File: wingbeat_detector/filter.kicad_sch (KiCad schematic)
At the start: 17 parts, among them J2 CONN_UMC_JACK_SMD, U2 UAF42_SMA

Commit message: Finished layout for v3.0
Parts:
- J2: value CONN_UMC_JACK_SMD -> UMC_JACK_SMD
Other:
- company: Howard Hughes Medical Institute -> Peter Polidoro
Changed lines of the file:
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@@
   (title_block
     (title "wingbeat_detector")
-    (date "2023-03-22")
+    (date "2023-03-23")
     (rev "3.0")
-    (company "Howard Hughes Medical Institute")
+    (company "Peter Polidoro")
   )
   (junction (at 106.68 50.8) (diameter 0) (color 0 0 0 0)
@@
       (effects (font (size 1.27 1.27)) (justify left))
     )
-    (property "Value" "CONN_UMC_JACK_SMD" (at 234.061 104.14 90)
-      (effects (font (size 1.27 1.27)) hide)
-    )
+    (property "Value" "UMC_JACK_SMD" (at 234.061 104.14 90)
+      (effects (font (size 1.27 1.27)) hide)
+    )

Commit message: More progress towards v4
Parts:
- removed RV1: 500k, Janelia:Potentiometer_Bourns_3223W_Vertical, symbol Janelia:R_Potentiometer_500k_3.9x3.18mm_11turn_Vertical
- added R14: GAIN1, Janelia:R_1206_3216Metric, symbol Janelia:R_150k_1206
- renumbered C9 to C6, C9 to C7, C9 to C8
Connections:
- net HIGHPASS_AMPLIFIED: now also R14.2
- net at R9.1, U2.6 (AAin-): now also R14.1
- no-connect marks 4 -> 3
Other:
- note added: "Vout/Vin = GAIN1 = Ra/Rb + 1 Low Gain: 5k/249 + 1 = 21 High Gain: 500k/249 + 1 = 2009"
- note removed: "Vout/Vin = Gain = Ra/Rb + 1 Min Gain: 5k/249 + 1 = 21 Max Gain: 500k/249 + 1 = 2009"
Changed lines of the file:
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@@
   (title_block
     (title "wingbeat_detector")
-    (date "2023-10-05")
+    (date "2023-12-08")
     (rev "4.0")
     (company "Peter Polidoro")
@@
   (junction (at 167.64 53.34) (diameter 0) (color 0 0 0 0)
   )
-  (junction (at 180.34 78.74) (diameter 0) (color 0 0 0 0)
-  )
-  (junction (at 180.34 154.94) (diameter 0) (color 0 0 0 0)
+  (junction (at 189.23 78.74) (diameter 0) (color 0 0 0 0)
+  )
+  (junction (at 189.23 154.94) (diameter 0) (color 0 0 0 0)
   )
   (no_connect (at 138.43 60.96))
-  (no_connect (at 177.8 53.34))
   (no_connect (at 101.6 85.09))
   (no_connect (at 101.6 161.29))
@@
     (stroke (width 0) (type default))
   )
-  (wire (pts (xy 180.34 46.99) (xy 180.34 78.74))
-    (stroke (width 0) (type default))
-  )
-  (wire (pts (xy 173.99 46.99) (xy 180.34 46.99))
+  (wire (pts (xy 189.23 53.34) (xy 189.23 78.74))
     (stroke (width 0) (type default))
   )
@@
     (stroke (width 0) (type default))
   )
-  (wire (pts (xy 157.48 154.94) (xy 180.34 154.94))
+  (wire (pts (xy 157.48 154.94) (xy 189.23 154.94))
     (stroke (width 0) (type default))
   )
@@
     (stroke (width 0) (type default))
   )
-  (wire (pts (xy 180.34 154.94) (xy 180.34 129.54))
+  (wire (pts (xy 189.23 154.94) (xy 189.23 129.54))
     (stroke (width 0) (type default))
   )
@@
     (stroke (width 0) (type default))
   )
-  (wire (pts (xy 157.48 78.74) (xy 180.34 78.74))
+  (wire (pts (xy 157.48 78.74) (xy 189.23 78.74))
     (stroke (width 0) (type default))
   )
@@
     (stroke (width 0) (type default))
   )
-  (wire (pts (xy 146.05 129.54) (xy 180.34 129.54))
+  (wire (pts (xy 146.05 129.54) (xy 189.23 129.54))
     (stroke (width 0) (type default))
   )
@@
     (stroke (width 0) (type default))
   )
+  (wire (pts (xy 182.88 53.34) (xy 189.23 53.34))
+    (stroke (width 0) (type default))
+  )
   (wire (pts (xy 72.39 86.36) (xy 72.39 83.82))
     (stroke (width 0) (type default))
   )
-  (wire (pts (xy 180.34 154.94) (xy 182.88 154.94))
+  (wire (pts (xy 189.23 154.94) (xy 191.77 154.94))
     (stroke (width 0) (type default))
   )
@@
     (stroke (width 0) (type default))
   )
-  (wire (pts (xy 180.34 78.74) (xy 182.88 78.74))
+  (wire (pts (xy 189.23 78.74) (xy 191.77 78.74))
     (stroke (width 0) (type default))
   )
@@
   )
   (wire (pts (xy 121.92 127) (xy 121.92 134.62))
-    (stroke (width 0) (type default))
-  )
-  (wire (pts (xy 173.99 46.99) (xy 173.99 49.53))
     (stroke (width 0) (type default))
   )
@@
     (effects (font (size 1.27 1.27)) (justify left bottom))
   )
-  (text "Vout/Vin = Gain = Ra/Rb + 1\nMin Gain: 5k/249 + 1 = 21\nMax Gain: 500k/249 + 1 = 2009 "
-    (at 166.37 44.45 0)
+  (text "Vout/Vin = GAIN1 = Ra/Rb + 1\nLow Gain: 5k/249 + 1 = 21\nHigh Gain: 500k/249 + 1 = 2009 "
+    (at 161.29 49.53 0)
     (effects (font (size 1.27 1.27)) (justify left bottom))
   )
@@
     (effects (font (size 1.27 1.27)) (justify left bottom))
   )
-  (label "BANDPASS_BUFFERED" (at 182.88 154.94 0) (fields_autoplaced)
+  (label "BANDPASS_BUFFERED" (at 191.77 154.94 0) (fields_autoplaced)
     (effects (font (size 1.27 1.27)) (justify left bottom))
   )
@@
     (effects (font (size 1.27 1.27)) (justify left bottom))
   )
-  (label "HIGHPASS_AMPLIFIED" (at 182.88 78.74 0) (fields_autoplaced)
+  (label "HIGHPASS_AMPLIFIED" (at 191.77 78.74 0) (fields_autoplaced)
     (effects (font (size 1.27 1.27)) (justify left bottom))
   )
@@
   (symbol (lib_id "Janelia:C_0.1uF_0402") (at 80.01 91.44 0) (unit 1)
     (in_bom yes) (on_board yes) (dnp no)
-    (property "Reference" "C9" (at 80.01 88.9 0)
+    (property "Reference" "C8" (at 80.01 88.9 0)
       (effects (font (size 1.016 1.016)) (justify left))
     )
@@
   (symbol (lib_id "Janelia:C_0.1uF_0402") (at 72.39 167.64 0) (unit 1)
     (in_bom yes) (on_board yes) (dnp no)
-    (property "Reference" "C9" (at 72.39 165.1 0)
+    (property "Reference" "C7" (at 72.39 165.1 0)
       (effects (font (size 1.016 1.016)) (justify left))
     )
@@
     )
   )
+  (symbol (lib_id "Janelia:R_150k_1206") (at 176.53 53.34 90) (unit 1)
+    (in_bom yes) (on_board yes) (dnp no)
+    (property "Reference" "R14" (at 176.53 50.8 90) (do_not_autoplace)
+      (effects (font (size 1.016 1.016)))
+    )
+    (property "Value" "GAIN1" (at 176.53 53.34 90) (do_not_autoplace)
+      (effects (font (size 0.762 0.762)))
+    )
+    (property "Footprint" "Janelia:R_1206_3216Metric" (at 176.53 55.118 90)
+      (effects (font (size 0.762 0.762)) hide)
+    )
+    (property "Datasheet" "" (at 176.53 51.308 90)
+      (effects (font (size 0.762 0.762)))
+    )
+    (property "Vendor" "Digi-Key" (at 173.99 48.768 90)
+      (effects (font (size 1.524 1.524)) hide)
+    )
+    (property "Vendor Part Number" "P150KBCCT-ND" (at 171.45 46.228 90)
+      (effects (font (size 1.524 1.524)) hide)
+    )
+    (property "Description" "RES SMD 150K OHM 0.1% 1/4W" (at 168.91 43.688 90)
+      (effects (font (size 1.524 1.524)) hide)
+    )
+    (property "Package" "1206" (at 176.53 53.34 0)
+      (effects (font (size 1.27 1.27)) hide)
+    )
+    (property "Manufacturer" "Panasonic Electronic Components" (at 176.53 53.34 0)
+      (effects (font (size 1.27 1.27)) hide)
+    )
+    (property "Manufacturer Part Number" "ERA-8AEB154V" (at 176.53 53.34 0)
+      (effects (font (size 1.27 1.27)) hide)
+    )
+    (pin "1")
+    (pin "2")
+    (instances
+      (project "wingbeat_detector"
+        (path "/cc457ebc-4af6-4663-b19f-8cb38f061cb4/6f9841bf-b0ef-48ff-bf2c-2bd611c72bf3"
+          (reference "R14") (unit 1)
+        )
+        (path "/cc457ebc-4af6-4663-b19f-8cb38f061cb4/6cde90e6-6156-42e3-aaac-c45ad2bfab8b"
+          (reference "R10") (unit 1)
+        )
+      )
+    )
+  )
   (symbol (lib_id "Janelia:R_49.9k_0402") (at 132.08 127 90) (unit 1)
     (in_bom yes) (on_board yes) (dnp no)
@@
     )
   )
-  (symbol (lib_id "Janelia:R_Potentiometer_500k_3.9x3.18mm_11turn_Vertical") (at 173.99 53.34 90) (unit 1)
-    (in_bom yes) (on_board yes) (dnp no)
-    (property "Reference" "RV1" (at 173.99 55.88 90)
-      (effects (font (size 1.27 1.27)))
-    )
-    (property "Value" "500k" (at 173.99 53.34 90)
-      (effects (font (size 1.27 1.27)))
-    )
-    (property "Footprint" "Janelia:Potentiometer_Bourns_3223W_Vertical" (at 156.21 53.34 0)
-      (effects (font (size 1.27 1.27)) hide)
-    )
-    (property "Datasheet" "~" (at 189.23 53.34 0)
-      (effects (font (size 1.27 1.27)) hide)
-    )
-    (property "Manufacturer" "Bourns Inc." (at 191.77 53.34 0)
-      (effects (font (size 1.27 1.27)) hide)
-    )
-    (property "Manufacturer Part Number" "3223W-1-504E" (at 158.75 53.34 0)
-      (effects (font (size 1.27 1.27)) hide)
-    )
-    (property "Description" "TRIMMER 500K OHM 0.125W J LEAD" (at 153.67 53.34 0)
-      (effects (font (size 1.27 1.27)) hide)
-    )
-    (property "Vendor" "Digi-Key" (at 186.69 53.34 0)
-      (effects (font (size 1.27 1.27)) hide)
-    )
-    (property "Vendor Part Number" "3223W-1-504ECT-ND" (at 161.29 53.34 0)
-      (effects (font (size 1.27 1.27)) hide)
-    )
-    (pin "1")
-    (pin "2")
-    (pin "3")
-    (instances
-      (project "wingbeat_detector"
-        (path "/cc457ebc-4af6-4663-b19f-8cb38f061cb4/6f9841bf-b0ef-48ff-bf2c-2bd611c72bf3"
-          (reference "RV1") (unit 1)
-        )
-        (path "/cc457ebc-4af6-4663-b19f-8cb38f061cb4/6cde90e6-6156-42e3-aaac-c45ad2bfab8b"
-          (reference "RV1") (unit 1)
-        )
-      )
-    )
-  )
   (symbol (lib_id "Janelia:C_0.1uF_0402") (at 72.39 91.44 0) (unit 1)
     (in_bom yes) (on_board yes) (dnp no)
-    (property "Reference" "C9" (at 72.39 88.9 0)
+    (property "Reference" "C6" (at 72.39 88.9 0)
       (effects (font (size 1.016 1.016)) (justify left))
     )

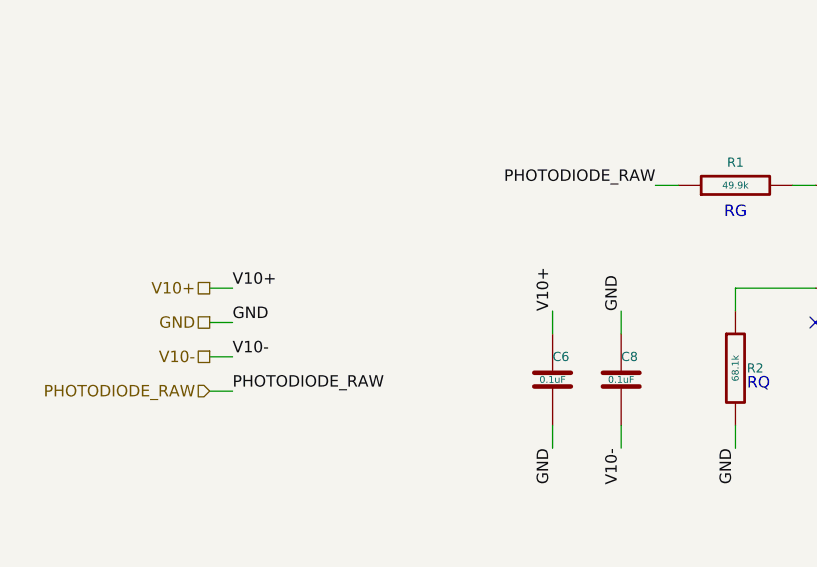
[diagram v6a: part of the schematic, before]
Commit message: Adjust tracks and zones
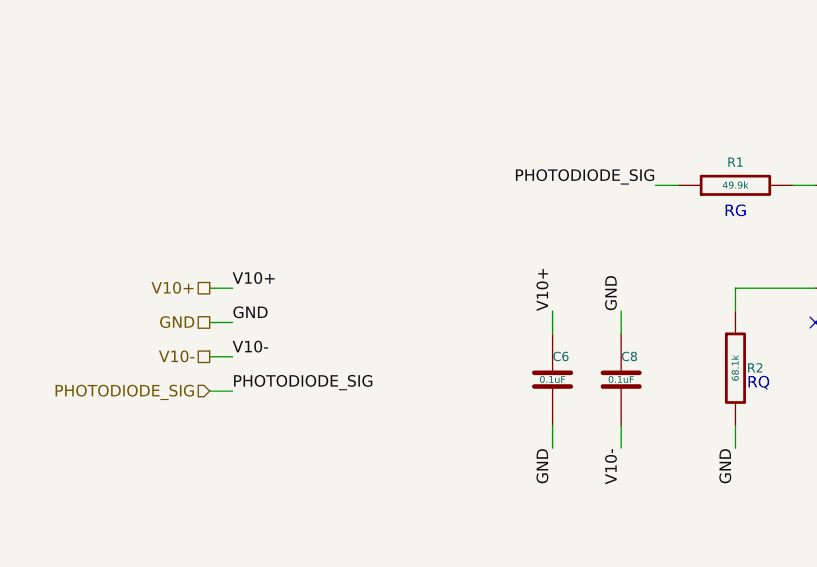
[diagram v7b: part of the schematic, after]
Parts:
- C6, C7, C8, C9: symbol Janelia:C_0.1uF_0402 -> Janelia:C_0.1uF_25V_0402
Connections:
- net PHOTODIODE_RAW renamed PHOTODIODE_SIG
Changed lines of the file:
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@@
   (title_block
     (title "wingbeat_detector")
-    (date "2023-12-11")
+    (date "2023-12-12")
     (rev "4.0")
     (company "Peter Polidoro")
@@
     (effects (font (size 1.27 1.27)) (justify right bottom))
   )
-  (label "PHOTODIODE_RAW" (at 83.82 69.85 180) (fields_autoplaced)
+  (label "PHOTODIODE_SIG" (at 83.82 69.85 180) (fields_autoplaced)
     (effects (font (size 1.27 1.27)) (justify right bottom))
   )
@@
     (effects (font (size 1.27 1.27)) (justify right bottom))
   )
-  (label "PHOTODIODE_RAW" (at 36.83 92.71 0) (fields_autoplaced)
+  (label "PHOTODIODE_SIG" (at 36.83 92.71 0) (fields_autoplaced)
     (effects (font (size 1.27 1.27)) (justify left bottom))
   )
@@
     (effects (font (size 1.27 1.27)) (justify right))
   )
-  (hierarchical_label "PHOTODIODE_RAW" (shape input) (at 34.29 92.71 180) (fields_autoplaced)
+  (hierarchical_label "PHOTODIODE_SIG" (shape input) (at 34.29 92.71 180) (fields_autoplaced)
     (effects (font (size 1.27 1.27)) (justify right))
   )
@@
     )
     (property "Manufacturer Part Number" "UAF42AU" (at 129.54 152.4 0)
+      (effects (font (size 1.27 1.27)) hide)
+    )
+    (property "Sim.Enable" "0" (at 129.54 152.4 0)
       (effects (font (size 1.27 1.27)) hide)
     )
@@
       (effects (font (size 1.27 1.27)) hide)
     )
+    (property "Sim.Enable" "0" (at 129.54 76.2 0)
+      (effects (font (size 1.27 1.27)) hide)
+    )
     (pin "1")
     (pin "10")
@@
       (effects (font (size 1.27 1.27)) hide)
     )
+    (property "Sim.Enable" "0" (at 231.14 104.14 0)
+      (effects (font (size 1.27 1.27)) hide)
+    )
     (pin "1")
     (pin "2")
@@
     )
   )
-  (symbol (lib_id "Janelia:C_0.1uF_0402") (at 80.01 167.64 0) (unit 1)
+  (symbol (lib_id "Janelia:C_0.1uF_25V_0402") (at 80.01 167.64 0) (unit 1)
     (in_bom yes) (on_board yes) (dnp no)
     (property "Reference" "C9" (at 80.01 165.1 0)
@@
     )
   )
-  (symbol (lib_id "Janelia:C_0.1uF_0402") (at 80.01 91.44 0) (unit 1)
+  (symbol (lib_id "Janelia:C_0.1uF_25V_0402") (at 80.01 91.44 0) (unit 1)
     (in_bom yes) (on_board yes) (dnp no)
     (property "Reference" "C8" (at 80.01 88.9 0)
@@
     )
   )
-  (symbol (lib_id "Janelia:C_0.1uF_0402") (at 72.39 167.64 0) (unit 1)
+  (symbol (lib_id "Janelia:C_0.1uF_25V_0402") (at 72.39 167.64 0) (unit 1)
     (in_bom yes) (on_board yes) (dnp no)
     (property "Reference" "C7" (at 72.39 165.1 0)
@@
     )
   )
-  (symbol (lib_id "Janelia:C_0.1uF_0402") (at 72.39 91.44 0) (unit 1)
+  (symbol (lib_id "Janelia:C_0.1uF_25V_0402") (at 72.39 91.44 0) (unit 1)
     (in_bom yes) (on_board yes) (dnp no)
     (property "Reference" "C6" (at 72.39 88.9 0)
